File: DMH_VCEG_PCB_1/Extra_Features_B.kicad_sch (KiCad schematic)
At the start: 38 parts, among them Q4 BC548, SW1 SW_DPDT_x2, U3 40106

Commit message: Placed Circuit B pages
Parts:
- renumbered C26 to C42, C27 to C43, D14 to D21, D9 to D22, D to D23, D11 to D24, D12 to D25, D13 to D26, Q4 to Q8, R133 to R135, R126 to R136, R127 to R137, R128 to R138, R129 to R139, R125 to R140, R2 to R141, R123 to R142, R4 to R143, R134 to R144, R117 to R55, R118 to R56, R119 to R57, R120 to R58, R132 to R59, R122 to R60, R121 to R61, R130 to R62, R131 to R63, R116 to R64, R124 to R65, SW1 to SW3, U to U10, U to U12, U3 to U14, U to U19
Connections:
- net Dec Logic: now also U12.12; no longer U12.13
- net GND: now also U10.10 (+), U10.12 (+), U19.10 (+); no longer U10.3 (+), U10.3 (+), U19.3 (+)
- net at R138.1, R64.1, R65.1: now also U12.11; no longer U12.1
- net at D22.1 (K): now also U12.10; no longer U12.2
- net at R140.2, R142.1: now also U19.8; no longer U19.1
- net at R140.1, R65.2: now also U19.9 (-); no longer U19.2 (-)
- net at R58.1, U19.1: now also U19.6 (-); no longer U19.2 (-)
- net at R135.1, R63.2: now also U10.13 (-); no longer U10.2 (-)
- net at R143.2, R144.1: now also U10.8; no longer U10.1
- net at R141.2, R143.1: now also U10.9 (-); no longer U10.2 (-)
- net at R135.2, R141.1: now also U10.14; no longer U10.1
- net at D22.2 (A): now also U19.7; no longer U19.1
- net at R60.2, R61.1: now also U19.5 (+); no longer U19.3 (+)
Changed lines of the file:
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@@
 		(lib_id "Analog_Switch:CD4066BE")
 		(at 127 101.6 180)
-		(unit 1)
+		(unit 4)
 		(exclude_from_sim no)
 		(in_bom yes)
@@
 		(dnp no)
 		(fields_autoplaced yes)
-		(property "Reference" "U"
+		(property "Reference" "U12"
 			(at 127 106.68 0)
 			(effects
@@
 		(on_board yes)
 		(dnp no)
-		(property "Reference" "C26"
+		(property "Reference" "C42"
 			(at 107.95 160.02 90)
 			(effects
@@
 		(on_board yes)
 		(dnp no)
-		(property "Reference" "D"
+		(property "Reference" "D23"
 			(at 178.1175 17.78 0)
 			(effects
@@
 		(on_board yes)
 		(dnp no)
-		(property "Reference" "R123"
+		(property "Reference" "R142"
 			(at 184.15 110.49 90)
 			(effects
@@
 		(dnp no)
 		(fields_autoplaced yes)
-		(property "Reference" "SW1"
+		(property "Reference" "SW3"
 			(at 120.65 156.21 0)
 			(effects
@@
 		(on_board yes)
 		(dnp no)
-		(property "Reference" "D11"
+		(property "Reference" "D24"
 			(at 178.1175 36.83 0)
 			(effects
@@
 		(on_board yes)
 		(dnp no)
-		(property "Reference" "R125"
+		(property "Reference" "R140"
 			(at 165.1 88.9 90)
 			(effects
@@
 		(on_board yes)
 		(dnp no)
-		(property "Reference" "R119"
+		(property "Reference" "R57"
 			(at 44.45 101.6 90)
 			(effects
@@
 		(on_board yes)
 		(dnp no)
-		(property "Reference" "U"
+		(property "Reference" "U19"
 			(at 65.278 96.266 0)
 			(effects
@@
 		(on_board yes)
 		(dnp no)
-		(property "Reference" "R132"
+		(property "Reference" "R59"
 			(at 69.85 177.8 90)
 			(effects
@@
 		(dnp no)
 		(fields_autoplaced yes)
-		(property "Reference" "#PWR062"
+		(property "Reference" "#PWR084"
 			(at 133.35 177.8 0)
 			(effects
@@
 		(on_board yes)
 		(dnp no)
-		(property "Reference" "R131"
+		(property "Reference" "R63"
 			(at 133.35 137.16 90)
 			(effects
@@
 		(on_board yes)
 		(dnp no)
-		(property "Reference" "R130"
+		(property "Reference" "R62"
 			(at 97.79 155.448 90)
 			(effects
@@
 		(on_board yes)
 		(dnp no)
-		(property "Reference" "R116"
+		(property "Reference" "R64"
 			(at 137.16 107.95 90)
 			(effects
@@
 		(on_board yes)
 		(dnp no)
-		(property "Reference" "R126"
+		(property "Reference" "R136"
 			(at 158.75 19.05 90)
 			(effects
@@
 		(dnp no)
 		(fields_autoplaced yes)
-		(property "Reference" "#PWR022"
+		(property "Reference" "#PWR081"
 			(at 50.8 114.3 0)
 			(effects
@@
 		(on_board yes)
 		(dnp no)
-		(property "Reference" "D13"
+		(property "Reference" "D26"
 			(at 178.1175 74.93 0)
 			(effects
@@
 		(dnp no)
 		(fields_autoplaced yes)
-		(property "Reference" "#PWR04"
+		(property "Reference" "#PWR088"
 			(at 175.26 160.02 0)
 			(effects
@@
 		(at 185.42 148.59 0)
 		(mirror x)
-		(unit 1)
+		(unit 3)
 		(exclude_from_sim no)
 		(in_bom yes)
 		(on_board yes)
 		(dnp no)
-		(property "Reference" "U"
+		(property "Reference" "U10"
 			(at 185.42 158.75 0)
 			(effects
@@
 		(on_board yes)
 		(dnp no)
-		(property "Reference" "Q4"
+		(property "Reference" "Q8"
 			(at 77.4701 156.21 0)
 			(effects
@@
 		(dnp no)
 		(fields_autoplaced yes)
-		(property "Reference" "#PWR025"
+		(property "Reference" "#PWR087"
 			(at 154.94 115.57 0)
 			(effects
@@
 		(on_board yes)
 		(dnp no)
-		(property "Reference" "R117"
+		(property "Reference" "R55"
 			(at 44.45 73.66 90)
 			(effects
@@
 		(at 152.4 146.05 0)
 		(mirror x)
-		(unit 1)
+		(unit 4)
 		(exclude_from_sim no)
 		(in_bom yes)
 		(on_board yes)
 		(dnp no)
-		(property "Reference" "U"
+		(property "Reference" "U10"
 			(at 152.4 156.21 0)
 			(effects
@@
 		(at 101.6 101.6 0)
 		(mirror x)
-		(unit 1)
+		(unit 2)
 		(exclude_from_sim no)
 		(in_bom yes)
 		(on_board yes)
 		(dnp no)
-		(property "Reference" "U"
+		(property "Reference" "U19"
 			(at 101.6 111.76 0)
 			(effects
@@
 		(on_board yes)
 		(dnp no)
-		(property "Reference" "R121"
+		(property "Reference" "R61"
 			(at 95.25 114.3 90)
 			(effects
@@
 		(on_board yes)
 		(dnp no)
-		(property "Reference" "R127"
+		(property "Reference" "R137"
 			(at 158.75 38.1 90)
 			(effects
@@
 		(dnp no)
 		(fields_autoplaced yes)
-		(property "Reference" "#PWR"
+		(property "Reference" "#PWR082"
 			(at 76.2 105.41 0)
 			(effects
@@
 		(dnp no)
 		(fields_autoplaced yes)
-		(property "Reference" "D9"
+		(property "Reference" "D22"
 			(at 114.3 95.25 0)
 			(effects
@@
 		(on_board yes)
 		(dnp no)
-		(property "Reference" "C27"
+		(property "Reference" "C43"
 			(at 107.061 172.72 90)
 			(effects
@@
 		(on_board yes)
 		(dnp no)
-		(property "Reference" "R133"
+		(property "Reference" "R135"
 			(at 152.4 127 90)
 			(effects
@@
 		(on_board yes)
 		(dnp no)
-		(property "Reference" "R124"
+		(property "Reference" "R65"
 			(at 149.86 107.95 90)
 			(effects
@@
 		(on_board yes)
 		(dnp no)
-		(property "Reference" "D12"
+		(property "Reference" "D25"
 			(at 178.1175 55.88 0)
 			(effects
@@
 		(at 165.1 104.14 0)
 		(mirror x)
-		(unit 1)
+		(unit 3)
 		(exclude_from_sim no)
 		(in_bom yes)
 		(on_board yes)
 		(dnp no)
-		(property "Reference" "U"
+		(property "Reference" "U19"
 			(at 165.1 114.3 0)
 			(effects
@@
 		(on_board yes)
 		(dnp no)
-		(property "Reference" "R120"
+		(property "Reference" "R58"
 			(at 63.5 73.66 90)
 			(effects
@@
 		(dnp no)
 		(fields_autoplaced yes)
-		(property "Reference" "U3"
+		(property "Reference" "U14"
 			(at 35.56 143.51 0)
 			(effects
@@
 		(dnp no)
 		(fields_autoplaced yes)
-		(property "Reference" "U3"
+		(property "Reference" "U14"
 			(at 53.34 143.51 0)
 			(effects
@@
 		(on_board yes)
 		(dnp no)
-		(property "Reference" "R128"
+		(property "Reference" "R138"
 			(at 158.75 57.15 90)
 			(effects
@@
 		(on_board yes)
 		(dnp no)
-		(property "Reference" "R122"
+		(property "Reference" "R60"
 			(at 82.55 110.49 90)
 			(effects
@@
 		(dnp no)
 		(fields_autoplaced yes)
-		(property "Reference" "#PWR063"
+		(property "Reference" "#PWR085"
 			(at 140.97 157.48 0)
 			(effects
@@
 		(on_board yes)
 		(dnp no)
-		(property "Reference" "R2"
+		(property "Reference" "R141"
 			(at 171.45 139.7 90)
 			(effects
@@
 		(on_board yes)
 		(dnp no)
-		(property "Reference" "R134"
+		(property "Reference" "R144"
 			(at 199.39 154.94 90)
 			(effects
@@
 		(dnp no)
 		(fields_autoplaced yes)
-		(property "Reference" "D14"
+		(property "Reference" "D21"
 			(at 76.2 139.7 0)
 			(effects
@@
 		(dnp no)
 		(fields_autoplaced yes)
-		(property "Reference" "#PWR023"
+		(property "Reference" "#PWR083"
 			(at 88.9 127 0)
 			(effects
@@
 		(on_board yes)
 		(dnp no)
-		(property "Reference" "R129"
+		(property "Reference" "R139"
 			(at 158.75 76.2 90)
 			(effects
@@
 		(on_board yes)
 		(dnp no)
-		(property "Reference" "R4"
+		(property "Reference" "R143"
 			(at 185.42 127 90)
 			(effects
@@
 		(on_board yes)
 		(dnp no)
-		(property "Reference" "R118"
+		(property "Reference" "R56"
 			(at 44.45 85.09 90)
 			(effects
@@
 		(dnp no)
 		(fields_autoplaced yes)
-		(property "Reference" "#PWR"
+		(property "Reference" "#PWR086"
 			(at 143.51 119.38 0)
 			(effects

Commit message: Reanotated schematic
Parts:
- removed C42: 1uF, Capacitor_THT:C_Disc_D4.3mm_W1.9mm_P5.00mm, symbol Device:C
- removed C43: 10uF, Capacitor_THT:CP_Radial_D5.0mm_P2.00mm, symbol Device:C_Polarized
- removed R55, R56, R57, R58, R60, R63, R64, R65: 100k, Resistor_THT:R_Axial_DIN0207_L6.3mm_D2.5mm_P7.62mm_Horizontal, symbol Device:R_US
- removed R59: 470R, Resistor_THT:R_Axial_DIN0207_L6.3mm_D2.5mm_P7.62mm_Horizontal, symbol Device:R_US
- removed R61: 100R, Resistor_THT:R_Axial_DIN0207_L6.3mm_D2.5mm_P7.62mm_Horizontal, symbol Device:R_US
- removed R62: 680R, Resistor_THT:R_Axial_DIN0207_L6.3mm_D2.5mm_P7.62mm_Horizontal, symbol Device:R_US
- removed SW3: SW_DPDT_x2, symbol Switch:SW_DPDT_x2
- removed U10: TL074, symbol Amplifier_Operational:TL074
- removed U12: CD4066BE, Package_DIP:DIP-14_W7.62mm, symbol Analog_Switch:CD4066BE
- removed U14: 40106, symbol 4xxx:40106
- removed U19: TL074, Package_DIP:DIP-14_W7.62mm_Socket, symbol Amplifier_Operational:TL074
- added C21: 1uF, Capacitor_THT:C_Disc_D4.3mm_W1.9mm_P5.00mm, symbol Device:C
- added C22: 10uF, Capacitor_THT:CP_Radial_D5.0mm_P2.00mm, symbol Device:C_Polarized
- added R124, R125, R126, R127, R129, R132, R133, R134: 100k, Resistor_THT:R_Axial_DIN0207_L6.3mm_D2.5mm_P7.62mm_Horizontal, symbol Device:R_US
- added R128: 470R, Resistor_THT:R_Axial_DIN0207_L6.3mm_D2.5mm_P7.62mm_Horizontal, symbol Device:R_US
- added R130: 100R, Resistor_THT:R_Axial_DIN0207_L6.3mm_D2.5mm_P7.62mm_Horizontal, symbol Device:R_US
- added R131: 680R, Resistor_THT:R_Axial_DIN0207_L6.3mm_D2.5mm_P7.62mm_Horizontal, symbol Device:R_US
- added SW2: SW_DPDT_x2, SynthStuff:Toggle_Switch_2_Poles_TE, symbol Switch:SW_DPDT_x2
- added U11, U18: TL074, Package_DIP:DIP-14_W7.62mm_Socket, symbol Amplifier_Operational:TL074
- added U13: CD4066BE, Package_DIP:DIP-14_W7.62mm, symbol Analog_Switch:CD4066BE
- added U15: 40106, Package_DIP:DIP-14_W7.62mm_Socket, symbol 4xxx:40106
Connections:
- net +12V: now also R129.1
- net Dec Logic: now also U13.12
- net Env Out: now also R124.2
- net GND: now also C21.2, R126.2, R130.2, R133.2, SW2.6 (C), U11.10 (+), U11.12 (+), U18.10 (+)
- net Proc Gate: now also U15.3
- net Rel Proc CV: now also R128.1
- net Sus Level: now also R125.1
- net at D22.1 (K): now also U13.10
- net at R138.1: now also R133.1, R134.1, U13.11
- net at R140.2, R142.1: now also U18.8
- net at R140.1: now also R134.2, U18.9 (-)
- net at Q8.2 (B): now also R128.2
- net at R135.1: now also R132.2, U11.13 (-)
- net at D21.1 (K), Q8.1 (C): now also R131.2
- net at R143.2, R144.1: now also U11.8
- net at R141.2, R143.1: now also U11.9 (-)
- net at D21.2 (A), Q8.3 (E): now also U15.6
- net at R135.2, R141.1: now also U11.14
- net at D22.2 (A): now also U18.7
- new net: R129.2, R130.1, U18.5 (+)
- new net: C21.1, C22.1, R131.1, R132.1
- new net: R127.1, U18.1, U18.6 (-)
- new net: R124.1, R127.2, U18.2 (-)
- new net: U15.4, U15.5
- new net: C22.2, SW2.5 (B)
- new net: R125.2, R126.1, U18.3 (+)

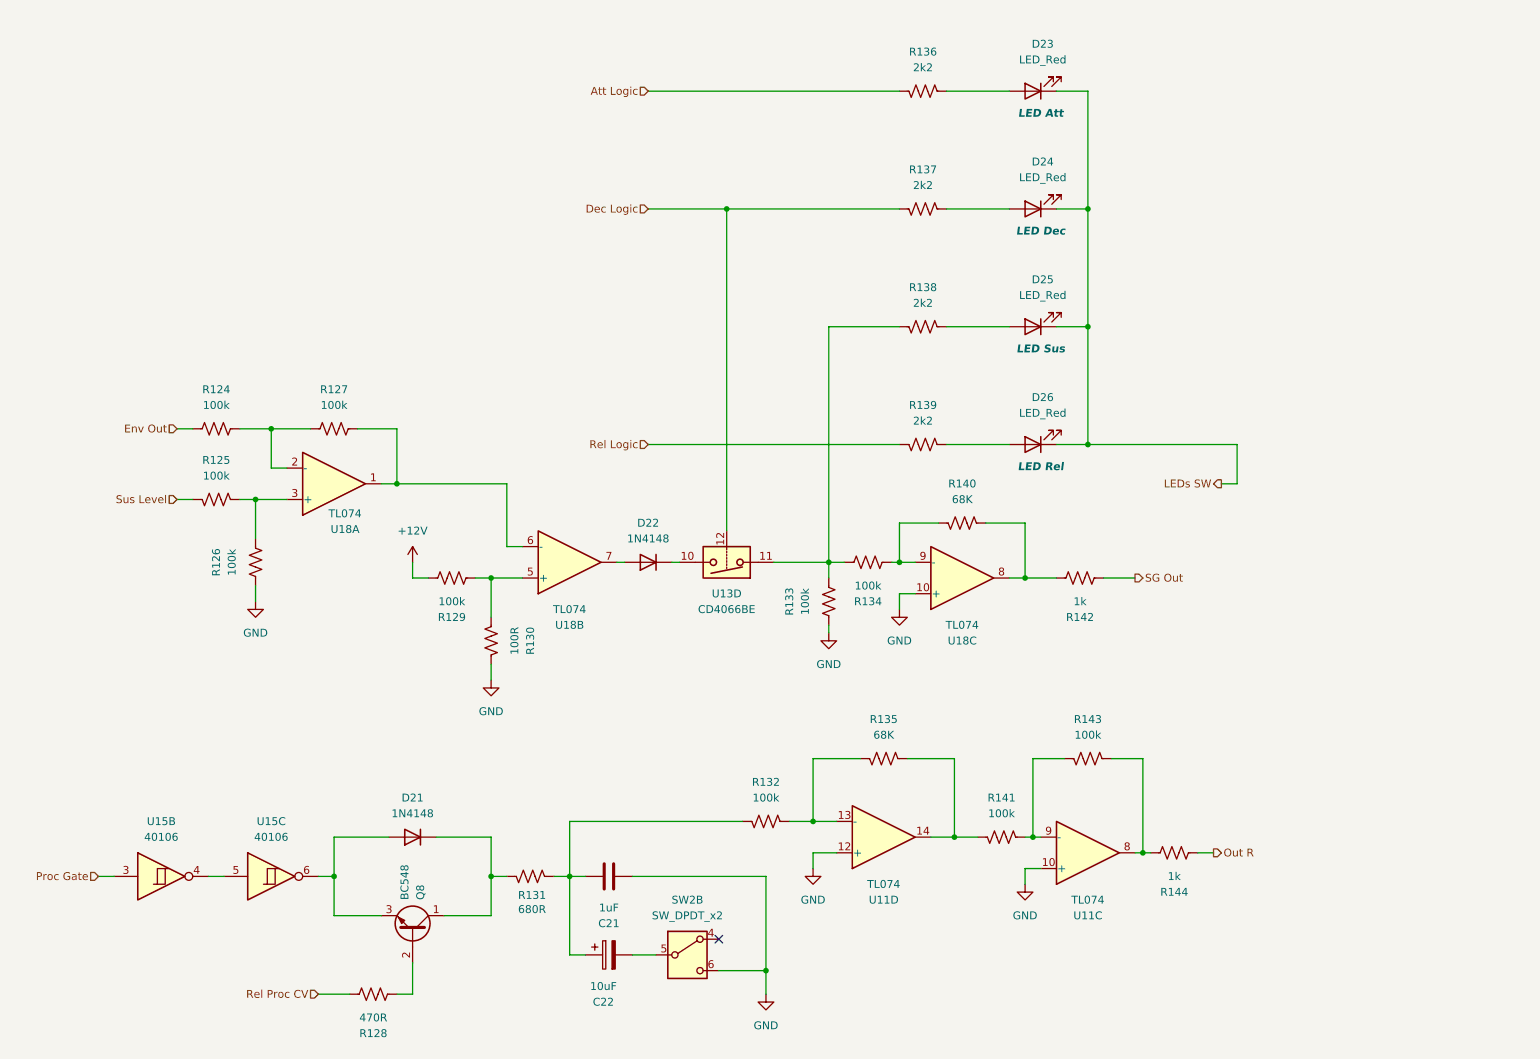
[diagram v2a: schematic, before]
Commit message: Reannotated ICs to match MFOS schematic
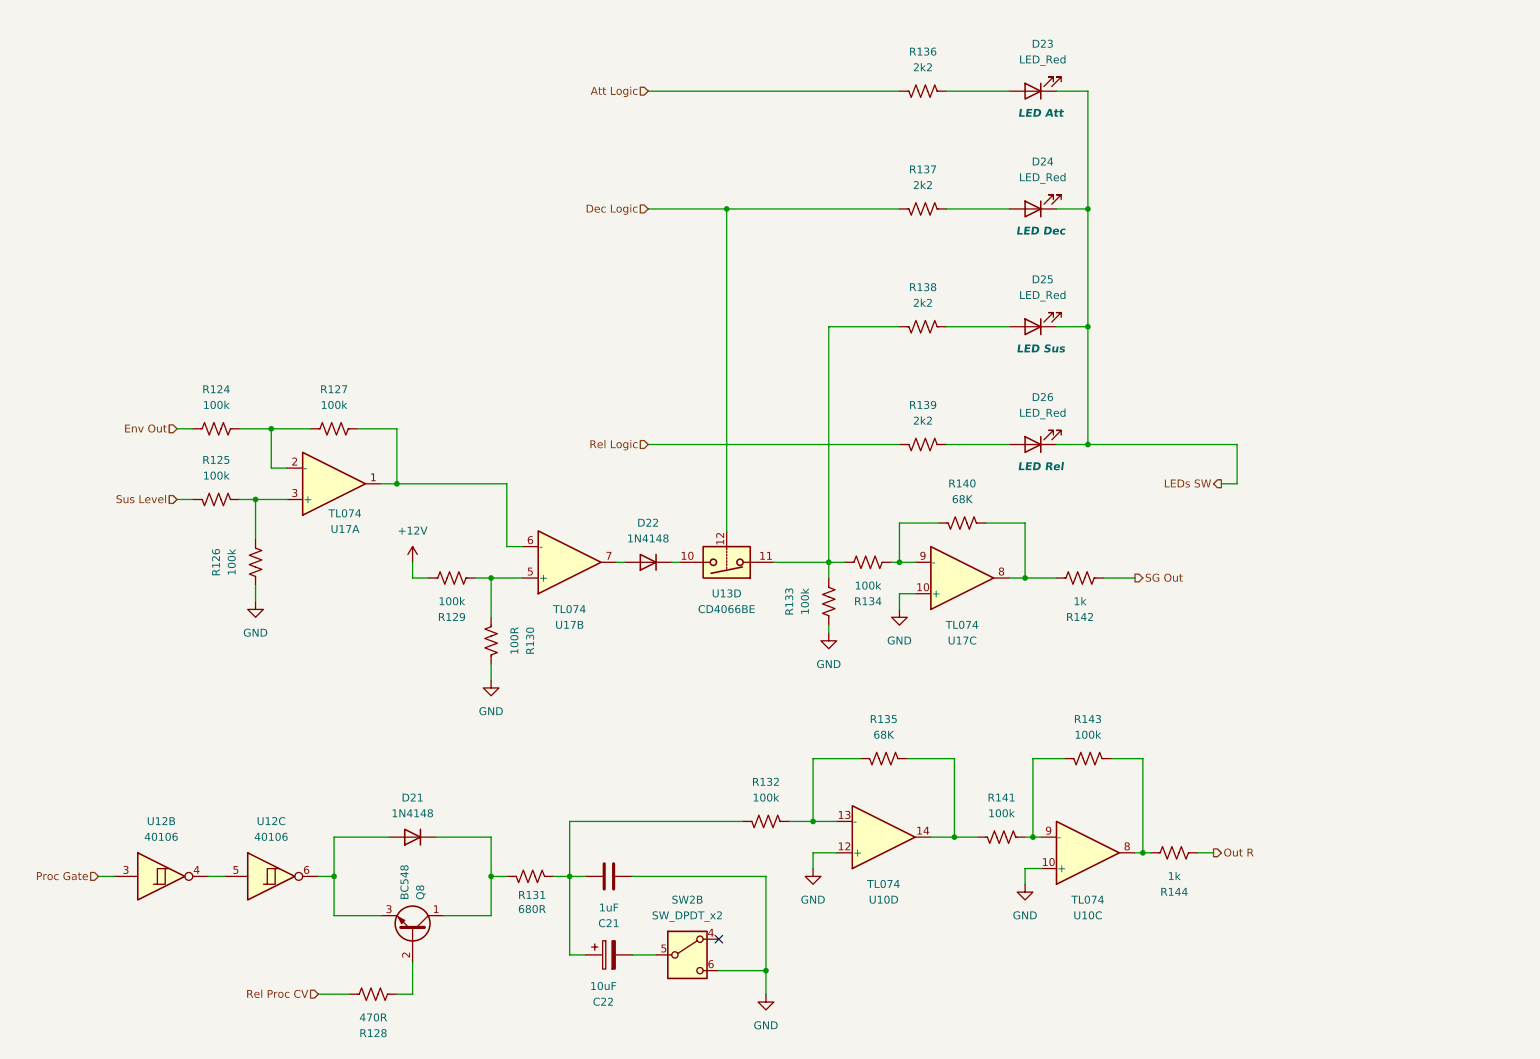
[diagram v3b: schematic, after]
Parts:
- renumbered U11 to U10, U15 to U12, U18 to U17
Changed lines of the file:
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@@
 		(dnp no)
 		(fields_autoplaced yes)
-		(property "Reference" "U15"
+		(property "Reference" "U12"
 			(at 53.34 143.51 0)
 			(effects
@@
 			)
 		)
+		(property "Function" ""
+			(at 53.34 152.4 0)
+			(effects
+				(font
+					(size 1.27 1.27)
+				)
+			)
+		)
 		(pin "7"
 		)
@@
 			(project "DMH_VCEG_PCB_1"
 				(path "/58f4306d-5387-4983-bb08-41a2313fd315/5112ef52-02ff-4071-9179-b1c0d55d0b73"
-					(reference "U15")
+					(reference "U12")
 					(unit 3)
 				)
@@
 		(on_board yes)
 		(dnp no)
-		(property "Reference" "U18"
+		(property "Reference" "U17"
 			(at 101.6 111.76 0)
 			(effects
@@
 			(project "DMH_VCEG_PCB_1"
 				(path "/58f4306d-5387-4983-bb08-41a2313fd315/5112ef52-02ff-4071-9179-b1c0d55d0b73"
-					(reference "U18")
+					(reference "U17")
 					(unit 2)
 				)
@@
 		(on_board yes)
 		(dnp no)
-		(property "Reference" "U11"
+		(property "Reference" "U10"
 			(at 152.4 156.21 0)
 			(effects
@@
 			(project "DMH_VCEG_PCB_1"
 				(path "/58f4306d-5387-4983-bb08-41a2313fd315/5112ef52-02ff-4071-9179-b1c0d55d0b73"
-					(reference "U11")
+					(reference "U10")
 					(unit 4)
 				)
@@
 		(on_board yes)
 		(dnp no)
-		(property "Reference" "U18"
+		(property "Reference" "U17"
 			(at 65.278 96.266 0)
 			(effects
@@
 			(project "DMH_VCEG_PCB_1"
 				(path "/58f4306d-5387-4983-bb08-41a2313fd315/5112ef52-02ff-4071-9179-b1c0d55d0b73"
-					(reference "U18")
+					(reference "U17")
 					(unit 1)
 				)
@@
 		(dnp no)
 		(fields_autoplaced yes)
-		(property "Reference" "U15"
+		(property "Reference" "U12"
 			(at 35.56 143.51 0)
 			(effects
@@
 			)
 		)
+		(property "Function" ""
+			(at 35.56 152.4 0)
+			(effects
+				(font
+					(size 1.27 1.27)
+				)
+			)
+		)
 		(pin "7"
 		)
@@
 			(project "DMH_VCEG_PCB_1"
 				(path "/58f4306d-5387-4983-bb08-41a2313fd315/5112ef52-02ff-4071-9179-b1c0d55d0b73"
-					(reference "U15")
+					(reference "U12")
 					(unit 2)
 				)
@@
 		(on_board yes)
 		(dnp no)
-		(property "Reference" "U11"
+		(property "Reference" "U10"
 			(at 185.42 158.75 0)
 			(effects
@@
 			(project "DMH_VCEG_PCB_1"
 				(path "/58f4306d-5387-4983-bb08-41a2313fd315/5112ef52-02ff-4071-9179-b1c0d55d0b73"
-					(reference "U11")
+					(reference "U10")
 					(unit 3)
 				)
@@
 		(on_board yes)
 		(dnp no)
-		(property "Reference" "U18"
+		(property "Reference" "U17"
 			(at 165.1 114.3 0)
 			(effects
@@
 			(project "DMH_VCEG_PCB_1"
 				(path "/58f4306d-5387-4983-bb08-41a2313fd315/5112ef52-02ff-4071-9179-b1c0d55d0b73"
-					(reference "U18")
+					(reference "U17")
 					(unit 3)
 				)
